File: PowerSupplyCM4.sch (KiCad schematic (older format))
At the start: 77 parts, among them J10 BAT, J11 IGNITION, Q1 SQJ461EP-T1-GE3, Q2 NVMFS5C442NL, Q3 SQD50P06-15L_GE3, Q4 SQ2362ES-T1_GE3, U10 TPS57114CQRTERQ1, U3 LM74610-Q1, U4 TLVH431AQDBVRQ1, U5 NSL-32, U6 LM53635LQRNL*Q1, U7 NSL-32, U8 TPS62293TDRVRQ1, U9 NSL-32

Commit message: - CM3 durch CM4 ersetzt - Spannungsregler für 3,3 und 1,8V entfernt, da nun von CM4 erzeugt - RTC IC getauscht
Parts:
- removed C38, C45, C46: 10u/10V/X7R, Capacitor_SMD:C_0805_2012Metric, symbol Device:C
- removed C39, C43, C44, C47, C48: 47u/6V3/X5R, Capacitor_SMD:C_1210_3225Metric, symbol Device:C
- removed C41, C42: 100n/50V/X7R, Capacitor_SMD:C_0603_1608Metric, symbol Device:C
- removed C49: NA, Capacitor_SMD:C_0603_1608Metric, symbol Device:C
- removed C50: 2n2/50V/X7R, Capacitor_SMD:C_0603_1608Metric, symbol Device:C
- removed C51: 47p/100V/C0G/5%, Capacitor_SMD:C_0805_2012Metric, symbol Device:C
- removed C52: 2n4/50V/C0G/5%, Capacitor_SMD:C_0603_1608Metric, symbol Device:C
- removed C53: 10n/50V/X7R, Capacitor_SMD:C_0603_1608Metric, symbol Device:C
- removed L3: IHLP3232DZER2R2M11, TeKaDe:IHLP-3232DZ, symbol TeKaDe:IHLP3232DZER2R2M11
- removed L4: XFL4020-102MEB, TeKaDe:XLF4020, symbol TeKaDe:XFL4020-102MEB
- removed R23: 4R7/5%, Resistor_SMD:R_0805_2012Metric, symbol Device:R
- removed R24: 249k/1%, Resistor_SMD:R_0603_1608Metric, symbol Device:R
- removed R25: 100k/1%, Resistor_SMD:R_0603_1608Metric, symbol Device:R
- removed R26: 4k75/1%, Resistor_SMD:R_0603_1608Metric, symbol Device:R
- removed R27: 82k5/1%, Resistor_SMD:R_0603_1608Metric, symbol Device:R
- removed R28: 80k6/1%, Resistor_SMD:R_0603_1608Metric, symbol Device:R
- removed U10: TPS57114CQRTERQ1, TeKaDe:TI-PWQFN-N16-1EP, symbol TeKaDe:TPS57114QRTERQ1
- removed U8: TPS62293TDRVRQ1, TeKaDe:TI-WSON-6-1EP, symbol TeKaDe:TPS62293TDRVRQ1
- renumbered C29 to C51, C21 to C52, C25 to C53, C33 to C54, C30 to C55, C34 to C56, C24 to C57, C16 to C58, C40 to C59, C17 to C60, C20 to C61, C22 to C62, C28 to C63, C37 to C64, C26 to C65, C31 to C66, C35 to C67, C36 to C68, C32 to C69, C18 to C70, C23 to C71, C27 to C72, C19 to C73, D3 to D4, D4 to D6, D6 to D7, J10 to J11, J11 to J12, Q4 to Q3, Q3 to Q4, Q1 to Q5, R21 to R25, R15 to R26, R18 to R27, R16 to R28, R17 to R29, R13 to R30, R14 to R31, R19 to R32, R22 to R33, R20 to R34, U6 to U13, U4 to U14, U3 to U15, U9 to U16, U5 to U17, U7 to U18
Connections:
- net labels removed: 1.8V, 3.3V, VSNS
- wire segments 307 -> 207
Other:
- note removed: "1.8V / 1A fixed out\nFPWM aktiv -> f_sw immer 2,25 MHz\n\nAusgangsspannung Ripple: 0,31mV\nStormbedarf am Ausgang: 400mA\n(lt 20210617 Leistungsaufnahme.xlsx)\n\nSpule etwas überdimensioniert, 2u2 / 40mR / 2.6A würde reichen\n\n\nÄnderungen:\n22p C entfernt, nur bei adjustable Typen notwendig\n(Überprüft mit Webbench und DS vgl. S.3 / FB Pin Beschreibung)\nMode auf High -> FPWM Mode\nCout von 10u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"
- note removed: "1u / 11mR / 5A"
- note removed: "3.3V / 3A\nR an RT/CLK = 82k5 -> f_sw 2,0 MHz\nC an SS/TR = 10n -> Slowstart Rate 4ms (Cout muss geladen werden)\n\nAusgangsspannung Ripple: 0,21mV\nStormbedarf am Ausgang: 800mA\n(lt 20210617 Leistungsaufnahme.xlsx)\n\nÄnderungen:\nFeedback R Toleranz auf 1% (war unnötigerweise 0,1)\nGND und GNDA getrennt"
- note removed: "COMP Beschaltung wie in Evalboard\nWebbench Designer liefert folgende Werte:\n(5k76 + 2n2) | 110p"
- note removed: "Max. 6VDC\n"
- note removed: "Tie the GND pins and AGND pin directly to the\nthermal pad under the IC. \n\nConnect the thermal pad to any internal PCB ground \nlanes using multiple vias directly under the IC."
- moved on the sheet: J12, R32, R33, R34

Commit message: - Selbsthalteschaltung vorerst fertig, Simulation folgt
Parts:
- removed D7: DIODE, symbol pspice:DIODE
- removed R33, R34: R, symbol Device:R
- removed U16, U17, U18: NSL-32, OptoDevice:Luna_NSL-32, symbol Isolator:NSL-32
- added D? (x2): 1N4148WQ-7-F, Diode_SMD:D_SOD-123F, symbol Device:D
- added R? (x3): 10k/1%, Resistor_SMD:R_0603_1608Metric, symbol Device:R
- added R?: 2k2/1%/250mW, symbol Device:R
- added U? (x2): VOMA617A, Package_SO:SOP-4_3.8x4.1mm_P2.54mm, symbol Isolator:PC817
- R32: value R -> 2k2/1%/250mW; footprint (none) -> Resistor_SMD:R_0603_1608Metric
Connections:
- net labels added: Ignition, PWRHold, PWR_ENABLE
- net labels removed: 5V_EN, 5V_EN_Coupled, Ignition_5V, Ignition_VPP
- wire segments 207 -> 215
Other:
- note added: "12V"
- note added: "5V"
- note added: "Aktivierung Buckconverter"
- note added: "Ermöglicht verzögertes Abschalten durch ATMEGA\n\nAus DS LM53635 S. 16:\nStart-up and shutdown of the LM53625/35-Q1 are controlled by the EN input. \nApplying a voltage of ≥ 2 V activates the device, while a voltage of ≤ 0.8 V is required to shut it down. \n(Max EN voltage: VIN)\nD.h. ATmega Ausgangspegel von 5V reicht für die Ansteuerung\nDas Zündungsignal muss aber auf 12V bleiben, da 5V nur ve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"
- note added: "OR Gate"
- note added: "Selbsthaltung Buckconverter"
- note added: "Signalisierung an ATMega"
- note removed: "Ermöglicht verzögertes Abschalten durch ATMEGA"
- moved on the sheet: J12, R32

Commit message: - Kleinigkeiten
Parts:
- added R?: 10k/1%, Resistor_SMD:R_0603_1608Metric, symbol Device:R
- R32, R?: value 2k2/1%/250mW -> 2k2/5%/250mW
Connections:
- net GND: now also R?.1
- net PWRHold: now also R?.2
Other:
- note added: "Bleibt ATmega GPIO auf GND wenn er sich Vcc selbst abdreht?\nFalls nicht, Pulldown ausreichend?"
- note added: "Ermöglicht verzögertes Abschalten durch ATMEGA\n\nAus DS LM53635 S. 16:\nStart-up and shutdown of the LM53625/35-Q1 are controlled by the EN input. \nApplying a voltage of ≥ 2 V activates the device, while a voltage of ≤ 0.8 V is required to shut it down. \n(Max EN voltage: 40V (wie VIN))\nD.h. ATmega Ausgangspegel von 5V reicht für die Ansteuerung\nDas Zündungsignal muss aber auf 12V bleiben, da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"
- note added: "Funktioniert \nnicht mit TTL"
- note removed: "Ermöglicht verzögertes Abschalten durch ATMEGA\n\nAus DS LM53635 S. 16:\nStart-up and shutdown of the LM53625/35-Q1 are controlled by the EN input. \nApplying a voltage of ≥ 2 V activates the device, while a voltage of ≤ 0.8 V is required to shut it down. \n(Max EN voltage: VIN)\nD.h. ATmega Ausgangspegel von 5V reicht für die Ansteuerung\nDas Zündungsignal muss aber auf 12V bleiben, da 5V nur ve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"
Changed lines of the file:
@@
 P 3100 12800
 F 0 "R32" V 2893 12800 50  0000 C CNN
-F 1 "2k2/1%/250mW" V 2984 12800 50  0000 C CNN
+F 1 "2k2/5%/250mW" V 2984 12800 50  0000 C CNN
 F 2 "Resistor_SMD:R_0603_1608Metric" V 3030 12800 50  0001 C CNN
 F 3 "~" H 3100 12800 50  0001 C CNN
@@
 P 3100 11750
 F 0 "R?" V 2893 11750 50  0000 C CNN
-F 1 "2k2/1%/250mW" V 2984 11750 50  0000 C CNN
+F 1 "2k2/5%/250mW" V 2984 11750 50  0000 C CNN
 F 2 "" V 3030 11750 50  0001 C CNN
 F 3 "~" H 3100 11750 50  0001 C CNN
@@
 	6050 13350 6050 13450
 Wire Wire Line
-	2400 13350 5400 13350
+	2400 13350 4250 13350
 Wire Wire Line
 	6050 13750 6050 13850
@@
 	5700 13350 6050 13350
 Text Notes 7300 13700 0    50   ~ 0
-Ermöglicht verzögertes Abschalten durch ATMEGA\n\nAus DS LM53635 S. 16:\nStart-up and shutdown of the LM53625/35-Q1 are controlled by the EN input. \nApplying a voltage of ≥ 2 V activates the device, while a voltage of ≤ 0.8 V is required to shut it down. \n(Max EN voltage: VIN)\nD.h. ATmega Ausgangspegel von 5V reicht für die Ansteuerung\nDas Zündungsignal muss aber auf 12V bleiben, da 5V nur verfügbar wenn alles an ist.\n\nÄnderungen:\n- Topologie geändert: OCs nun parallel an Ignition, statt in Reihe\n- ODER Schaltung um 2te Diode und Pulldown ergänzt\n- PWR_Enable an Buckconverter angeschlossen\n- Optokoppler für ATmega Ausgangssignal entfernt, da galv. Trennung hier unnötig\n- SMD Optokoppler\n- Nicht Invertierender Ausgang\n\nBerechnung Vorwiderstand OC:\nLED Vf  1,33 - 1,5 V @ 5mA (max 20mA)\nKFZ Spannung max ~14V\n=> R = (14V -1,4V) / 5mA = 2500\nWahl: 2k2, etwas mehr Strom, genug Sicherheit\n\n
+Ermöglicht verzögertes Abschalten durch ATMEGA\n\nAus DS LM53635 S. 16:\nStart-up and shutdown of the LM53625/35-Q1 are controlled by the EN input. \nApplying a voltage of ≥ 2 V activates the device, while a voltage of ≤ 0.8 V is required to shut it down. \n(Max EN voltage: 40V (wie VIN))\nD.h. ATmega Ausgangspegel von 5V reicht für die Ansteuerung\nDas Zündungsignal muss aber auf 12V bleiben, da 5V nur verfügbar wenn alles an ist.\n\nÄnderungen:\n- Topologie geändert: OCs nun parallel an Ignition, statt in Reihe\n- ODER Schaltung um 2te Diode und Pulldown ergänzt\n- PWR_Enable an Buckconverter angeschlossen\n- Optokoppler für ATmega Ausgangssignal entfernt, da galv. Trennung hier unnötig\n- SMD Optokoppler\n- Nicht Invertierender Ausgang\n\nBerechnung Vorwiderstand OC:\nLED Vf  1,33 - 1,5 V @ 5mA (max 20mA)\nKFZ Spannung max ~14V\n=> R = (14V -1,4V) / 5mA = 2500\nWahl: 2k2, etwas mehr Strom, genug Sicherheit\n\n
 Connection ~ 6050 13350
 Text Label 6500 13350 0    50   ~ 0
@@
 Text HLabel 2400 13350 0    50   Input ~ 0
 PWRHold
-Wire Wire Line
-	4150 13000 4550 13000
 $Comp
 L Device:R R?
@@
 Text Notes 2800 13350 0    50   ~ 0
 Selbsthaltung Buckconverter
+Text Notes 3000 14450 0    50   ~ 0
+Bleibt ATmega GPIO auf GND wenn er sich Vcc selbst abdreht?\nFalls nicht, Pulldown ausreichend?
+$Comp
+L Device:R R?
+U 1 1 616BB340
+P 4250 14900
+F 0 "R?" V 4043 14900 50  0000 C CNN
+F 1 "10k/1%" V 4134 14900 50  0000 C CNN
+F 2 "Resistor_SMD:R_0603_1608Metric" V 4180 14900 50  0001 C CNN
+F 3 "~" H 4250 14900 50  0001 C CNN
+	1    4250 14900
+	1    0    0    1
+$EndComp
+$Comp
+L power:GND #PWR?
+U 1 1 616BB34B
+P 4250 15200
+F 0 "#PWR?" H 4250 14950 50  0001 C CNN
+F 1 "GND" H 4255 15027 50  0000 C CNN
+F 2 "" H 4250 15200 50  0001 C CNN
+F 3 "" H 4250 15200 50  0001 C CNN
+	1    4250 15200
+	1    0    0    -1
+$EndComp
+Wire Wire Line
+	4250 15200 4250 15050
+Wire Wire Line
+	4150 13000 4550 13000
+Wire Wire Line
+	4250 13350 4250 14750
+Connection ~ 4250 13350
+Wire Wire Line
+	4250 13350 5400 13350
+Text Notes 5250 13950 0    50   ~ 0
+Funktioniert \nnicht mit TTL
 $EndSCHEMATC

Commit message: - ESD Schutz Zündung
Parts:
- added C? (x2): 4n7/100V/X7R, Capacitor_SMD:C_0805_2012Metric, symbol Device:C
- added C?: 10u/50V/X7R, Capacitor_SMD:C_1210_3225Metric, symbol Device:C
- added D?: SMBJ14A-13-F, Diode_SMD:D_SMB, symbol Device:D_Schottky
- added D?: SMBJ28A-13-F, Diode_SMD:D_SMB, symbol Device:D_Schottky
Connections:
- net -BATT: now also C?.2, C?.2, D?.1 (K)
- net at J12.1 (Pin_1), R32.2, R?.2: now also C?.1, C?.1, D?.1 (K)
- new net: C?.1, C?.2
- new net: D?.2 (A), D?.2 (A)
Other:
- note removed: "Steckverbinder KFZ Spannungseingang"
- moved on the sheet: D?, J12, R32, R?, U?

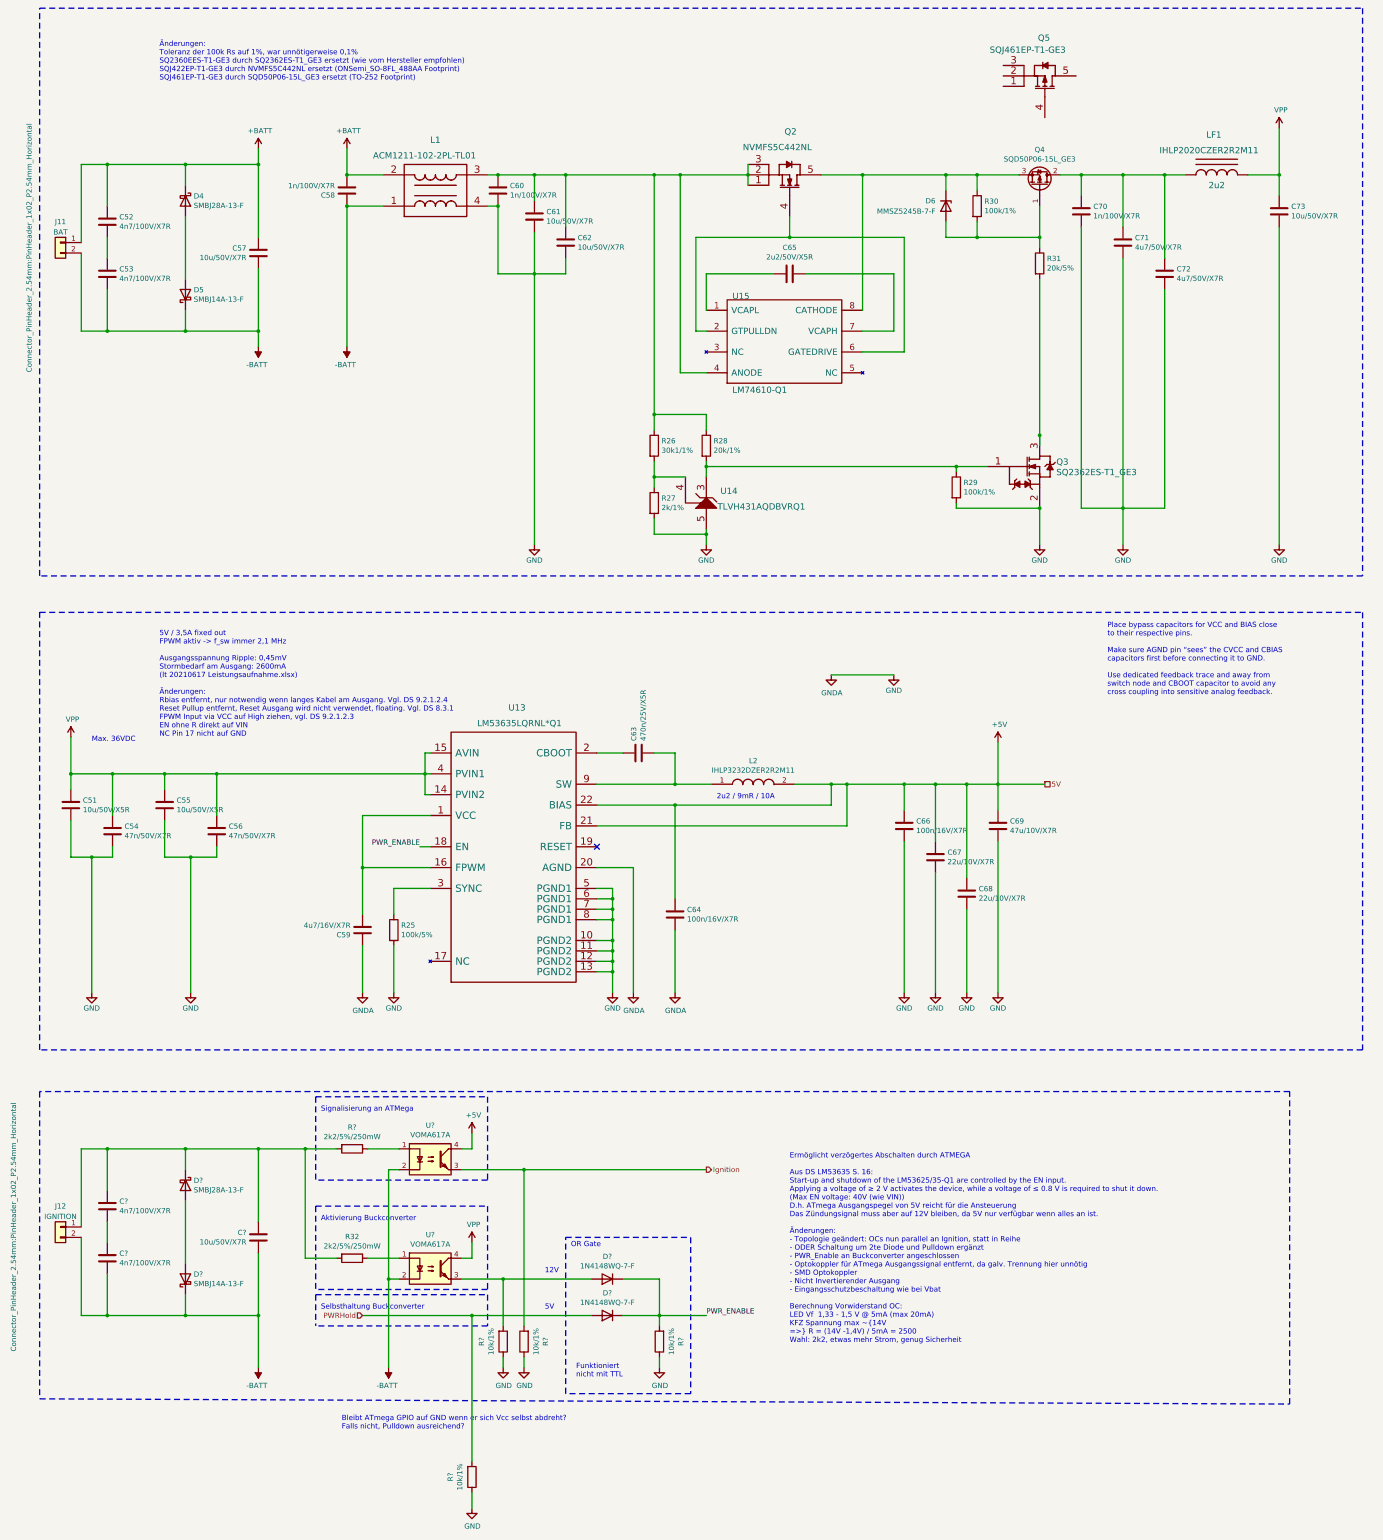
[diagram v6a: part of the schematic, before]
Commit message: - ATmega überarbeitet - Alle offenen Punkte zusammengefasst
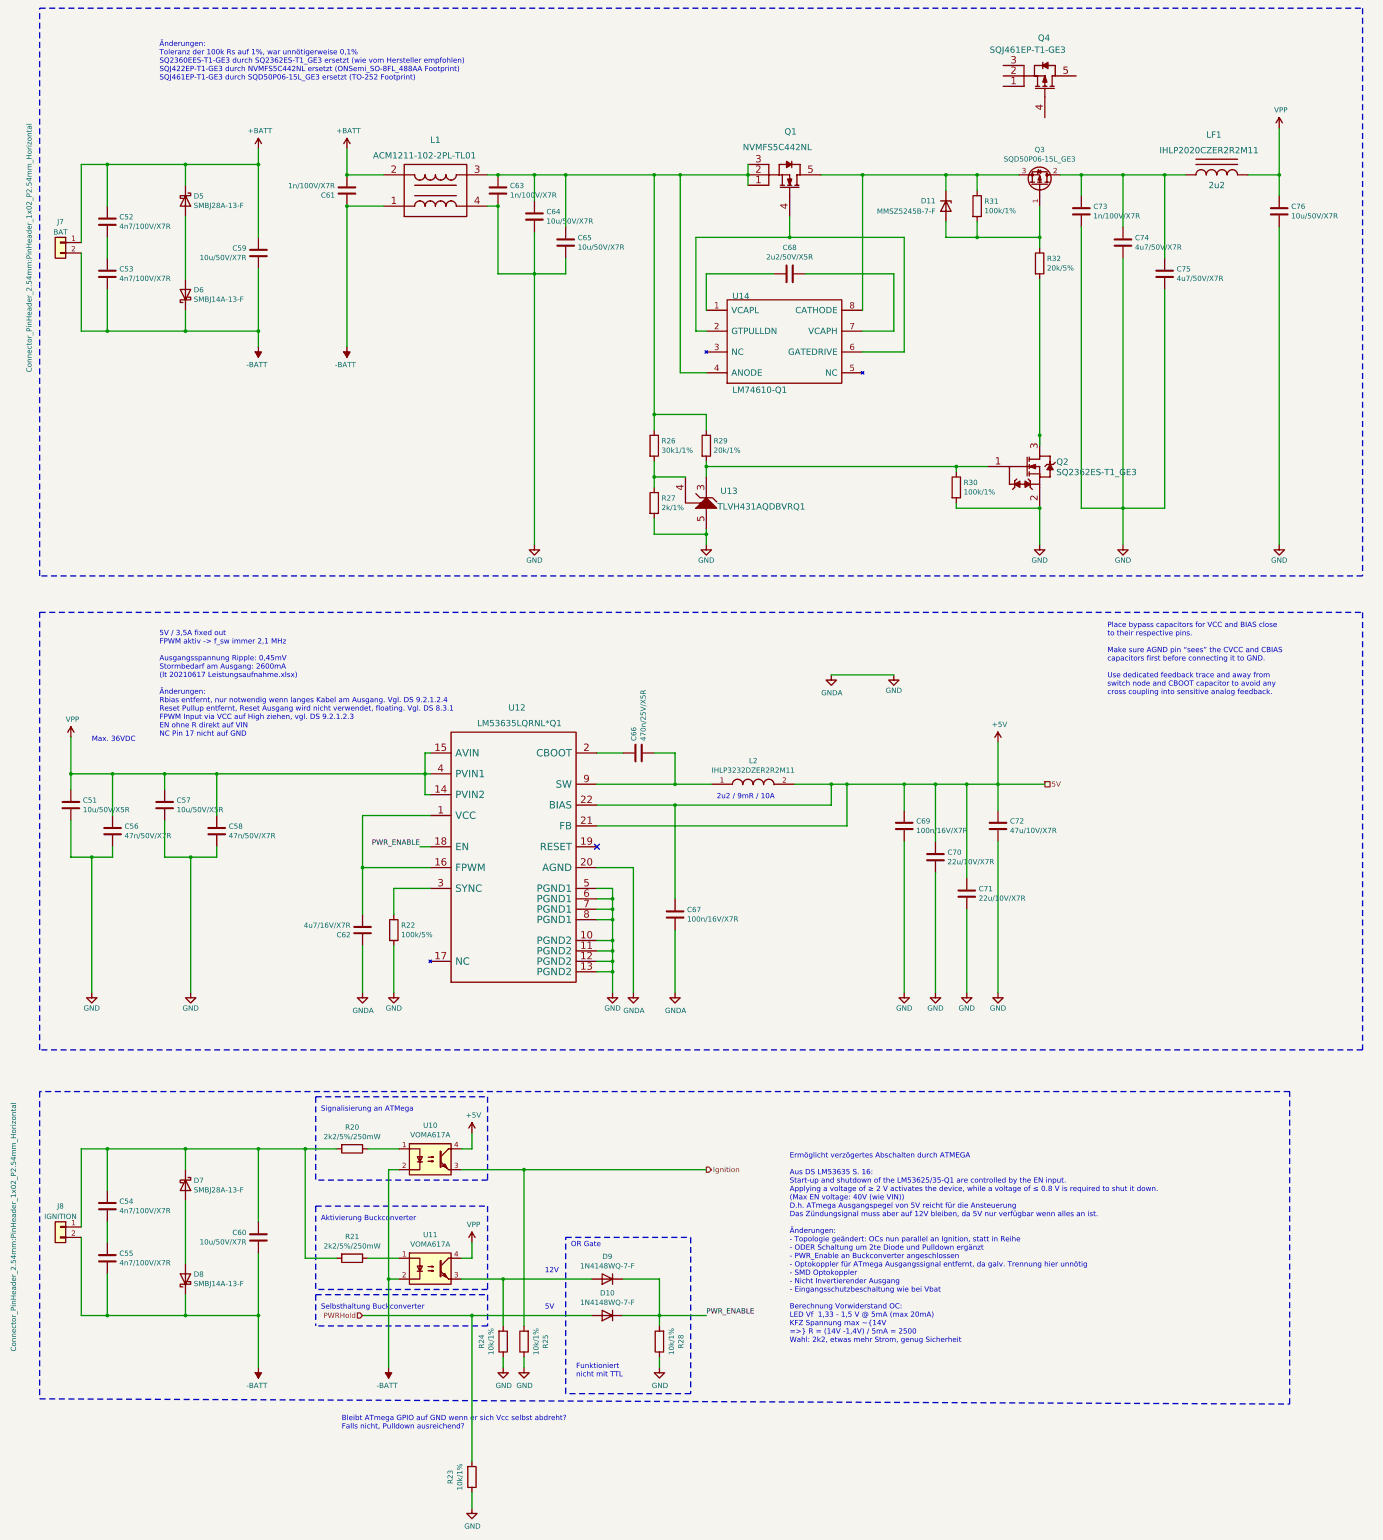
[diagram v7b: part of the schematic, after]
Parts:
- R20: renamed from R?; footprint (none) -> Resistor_SMD:R_0603_1608Metric
- gave numbers to parts that had none: 13
- renumbered C54 to C56, C55 to C57, C56 to C58, C57 to C59, C58 to C61, C59 to C62, C60 to C63, C61 to C64, C62 to C65, C63 to C66, C64 to C67, C65 to C68, C66 to C69, C67 to C70, C68 to C71, C69 to C72, C70 to C73, C71 to C74, C72 to C75, C73 to C76, D6 to D11, D4 to D5, D5 to D6, J11 to J7, J12 to J8, Q2 to Q1, Q3 to Q2, Q4 to Q3, Q5 to Q4, R32 to R21, R25 to R22, R28 to R29, R29 to R30, R30 to R31, R31 to R32, U13 to U12, U14 to U13, U15 to U14
